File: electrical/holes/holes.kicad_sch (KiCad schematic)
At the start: 16 parts, among them J1 GPIO, U1 CAT24C256, U2 MCP23017_SO

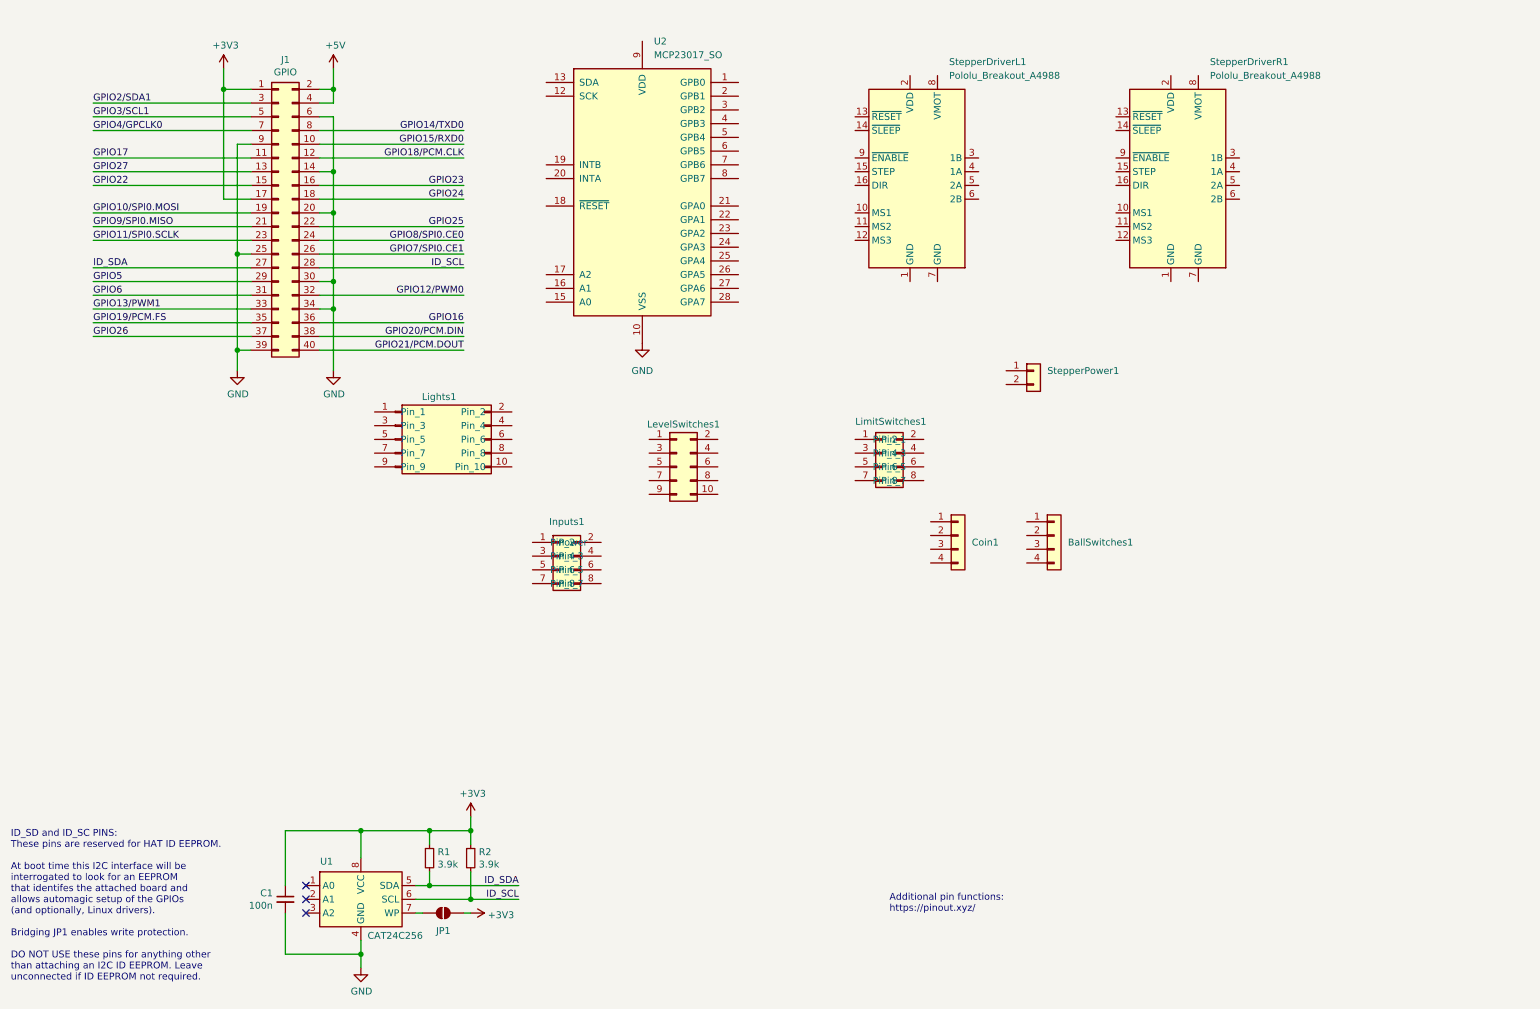
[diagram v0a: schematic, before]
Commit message: clean up schematic
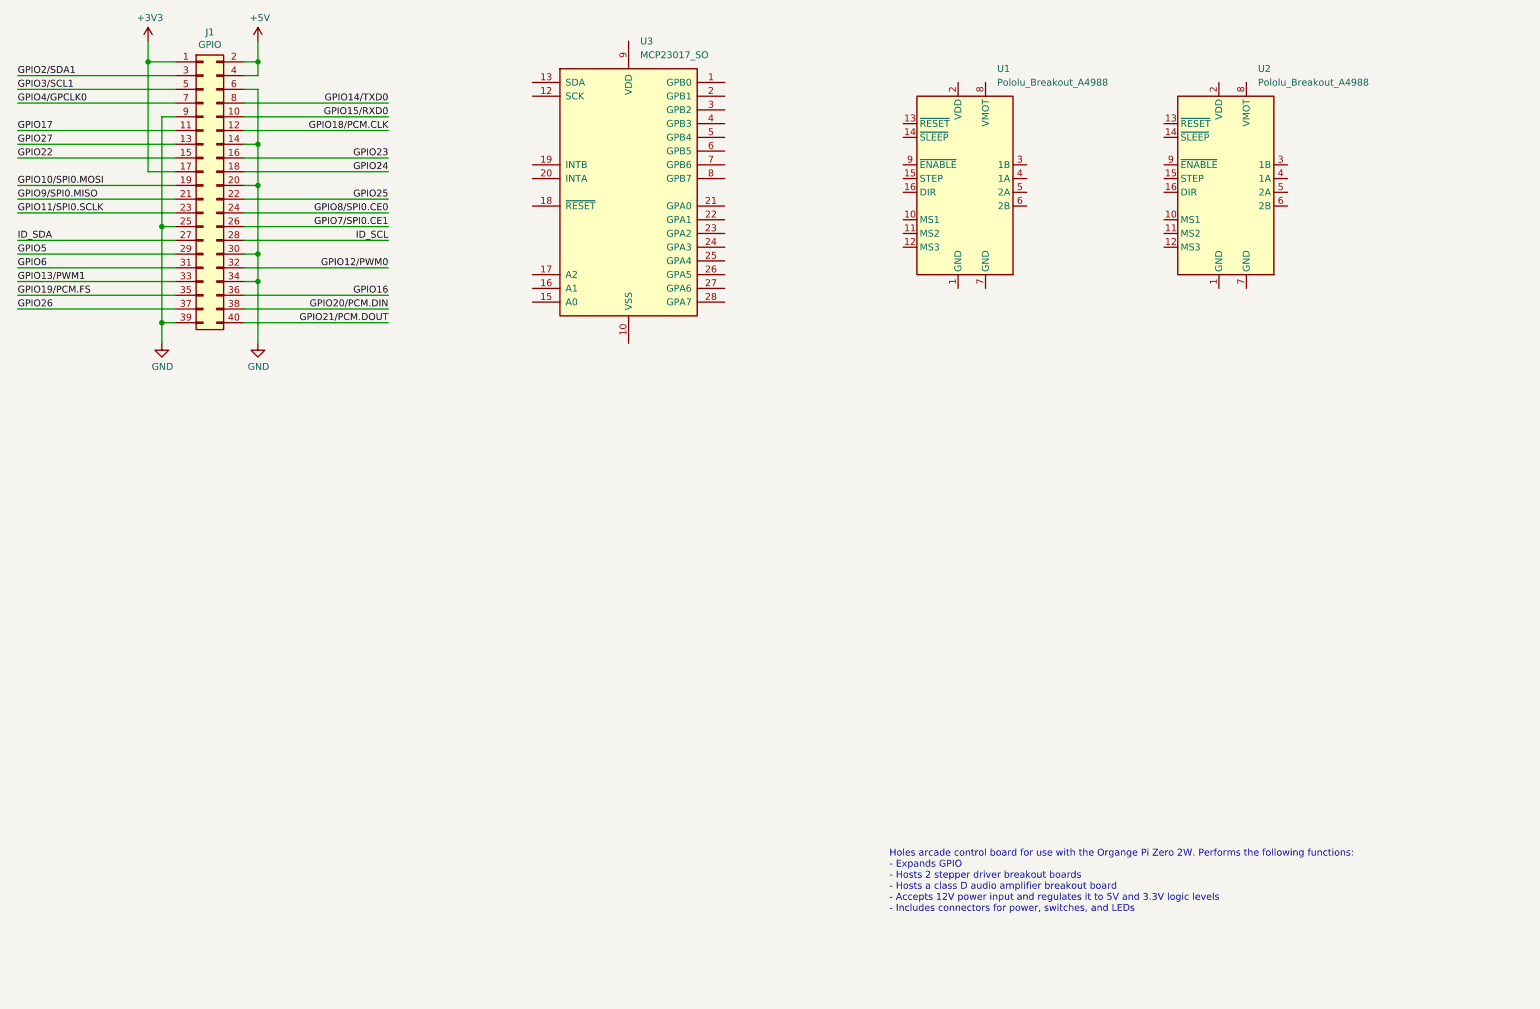
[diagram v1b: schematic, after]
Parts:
- removed BallSwitches1, Coin1: Conn_01x04, Connector_JST:JST_ZH_B4B-ZR_1x04_P1.50mm_Vertical, symbol Connector_Generic:Conn_01x04
- removed C1: 100n, symbol Device:C_Small
- removed Inputs1, LimitSwitches1: Conn_02x04_Odd_Even, Connector_JST:JST_PHD_B8B-PHDSS_2x04_P2.00mm_Vertical, symbol Connector_Generic:Conn_02x04_Odd_Even
- removed JP1: ID_WP, symbol Jumper:SolderJumper_2_Open
- removed LevelSwitches1, Lights1: Conn_02x05_Odd_Even, Connector_JST:JST_PHD_B10B-PHDSS_2x05_P2.00mm_Vertical, symbol Connector_Generic:Conn_02x05_Odd_Even
- removed R1, R2: 3.9k, symbol Device:R_Small
- removed StepperPower1: Conn_01x02, Connector_JST:JST_XH_B2B-XH-A_1x02_P2.50mm_Vertical, symbol Connector_Generic:Conn_01x02
- removed U1: CAT24C256, symbol Memory_EEPROM:CAT24C256
- J1: Notes (none) -> 27 and 28 reserved for I2C hat detection; Purpose (none) -> Main pi GPIO connection
- U1: renamed from StepperDriverL1; Purpose (none) -> Left stepper driver
- U2: renamed from StepperDriverR1; Purpose (none) -> Right stepper driver
- U3: renamed from U2; Purpose (none) -> GPIO expansion
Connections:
- net GND: no longer U3.10 (VSS)
- no-connect marks 3 -> 0
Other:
- note added: "Holes arcade control board for use with the Organge Pi Zero 2W. Performs the following functions: - Expands GPIO - Hosts 2 stepper driver breakout boards - Hosts a class D audio amplifier breakout board - Accepts 12V power input and regulates it to 5V and 3.3V logic levels - Includes connectors for power, switches, and LEDs"
- note removed: "Additional pin functions: https://pinout.xyz/"
- note removed: "ID_SD and ID_SC PINS: These pins are reserved for HAT ID EEPROM. At boot time this I2C interface will be interrogated to look for an EEPROM that identifes the attached board and allows automagic setup of the GPIOs (and optionally, Linux drivers). Bridging JP1 enables write protection. DO NOT USE these pins for anything other than attaching an I2C ID EEPROM. Leave unconnected if ID EEPROM not requ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"
- title: (none) -> Holes arcade control board
- moved on the sheet: J1, U1, U2, U3
